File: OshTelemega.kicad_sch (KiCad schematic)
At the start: 138 parts, among them J1 USB_C_Receptacle_USB2.0_16P, J10 SERVOS, J12 DEBUG, J2 Conn_02x04_Counter_Clockwise, J3 SMA_Edgelaunch, J4 USB_C_Receptacle_USB2.0_16P, J5 UFL, J6 RIGHT, J7 LEFT, J8 Conn_01x02, U1 STM32L151VCTx, U10 MMC5983MA, U11 TSM200N03, U12 LM293QT, U13 LM293QT, U14 TSM200N03, U15 LM293QT, U16 TSM200N03, U17 MCP73831-2-OT, U18 TC2185-3.3VxCTTR, U2 WE-TVS-82400102, U3 ADXL375, U4 MS5607-02BA, U5 MAX-M10S, U6 MCP130-xxxxTT, U7 W25Q64JVXGIQ, U8 CC1200, U9 BMI088, Y1 ABM8W-40.0000MHZ

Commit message: v0.1 done. Redesigning for potential mosaic integration
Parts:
- removed BZ1: Buzzer, Buzzer_Beeper:Buzzer_TDK_PS1240P02BT_D12.2mm_H6.5mm, symbol Device:Buzzer
- removed J1: USB_C_Receptacle_USB2.0_16P, Connector_USB:USB_C_Receptacle_GCT_USB4105-xx-A_16P_TopMnt_Horizontal, symbol Connector:USB_C_Receptacle_USB2.0_16P
- removed U7: W25Q64JVXGIQ, FCU2025Lib:DFN_XGIQ TR_WIN, symbol Memory_Flash:W25Q32JVSS
- added H5: MountingHole_Pad, MountingHole:MountingHole_3.2mm_M3_DIN965_Pad, symbol Mechanical:MountingHole_Pad
- added U19: W25Q64JVXGIQ, FCU2025Lib:DFN_XGIQ TR_WIN, symbol Memory_Flash:W25Q128JVP
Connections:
- net +3V3: now also U19.3 (~{WP}/IO_{2}), U19.7 (~{HOLD}/~{RESET}/IO_{3}), U19.8 (VCC)
- net CS_COMP0: now also J2.8 (Pin_8); no longer J2.6 (Pin_6)
- net CS_COMP1: now also J2.6 (Pin_6); no longer J2.5 (Pin_5)
- net CS_FLASH: now also U19.1 (~{CS})
- net FET_C: now also R27.1, U14.7_8 (D); no longer R23.1, U14.5_6 (D)
- net FET_D: now also R23.1, U14.5_6 (D); no longer R27.1, U14.7_8 (D)
- net FIRE_C: now also R25.2, R26.1; no longer R21.2, R22.1
- net FIRE_D: now also R21.2, R22.1; no longer R25.2, R26.1
- net GATE_C: now also R26.2, U14.2 (G); no longer R22.2, U14.4 (G)
- net GATE_D: now also R22.2, U14.4 (G); no longer R26.2, U14.2 (G)
- net GATE_E: now also U15.7 (OUT2); no longer U15.1 (OUT1)
- net GATE_F: now also U15.1 (OUT1); no longer U15.7 (OUT2)
- net GND: now also J4.A1 (GND), J4.A12 (GND), J4.B1 (GND), J4.B12 (GND), J4.S1 (SHIELD), H5.1, U19.4 (GND), U19.9 (EP)
- net MISO2: now also U19.2 (DO/IO_{1})
- net MOSI2: now also J2.5 (Pin_5), U19.5 (DI/IO_{0}); no longer J2.3 (Pin_3)
- net NRST: now also J12.4 (Pin_4); no longer J12.2 (Pin_2)
- net SCK2: now also U19.6 (CLK)
- net SENSE_C: now also R27.2, R28.2; no longer R23.2, R24.2
- net SENSE_D: now also R23.2, R24.2; no longer R27.2, R28.2
- net SWCLK: now also J12.2 (Pin_2); no longer J12.4 (Pin_4)
- net VBUS: now also J4.A4 (VBUS), J4.A9 (VBUS), J4.B4 (VBUS), J4.B9 (VBUS)
- net V_LIPO: now also J2.3 (Pin_3); no longer J2.8 (Pin_8)
- net at R1.1: now also J4.A5 (CC1)
- net at R10.1: now also J4.A6 (D+), J4.B6 (D+)
- net at R9.1: now also J4.A7 (D-), J4.B7 (D-)
- net at R2.1: now also J4.B5 (CC2)
- net at R6.2: now also J10.4 (Pin_4); no longer J10.3 (Pin_3)
- net at R7.2: now also J10.3 (Pin_3); no longer J10.4 (Pin_4)
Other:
- moved on the sheet: J4

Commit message: before adding 10 pin companion
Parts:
- removed J12: DEBUG, Connector_PinHeader_1.27mm:PinHeader_2x02_P1.27mm_Vertical, symbol Connector_Generic:Conn_02x02_Counter_Clockwise
- added J1: Conn_ARM_SWD_TagConnect_TC2030-NL, Connector:Tag-Connect_TC2030-IDC-NL_2x03_P1.27mm_Vertical, symbol Connector:Conn_ARM_SWD_TagConnect_TC2030-NL
- added J9: Conn_02x05_Counter_Clockwise, Connector_PinHeader_1.27mm:PinHeader_2x05_P1.27mm_Vertical, symbol Connector_Generic:Conn_02x05_Counter_Clockwise
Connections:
- net +3V3: now also J1.1 (VCC)
- net GND: now also J1.5 (GND)
- net NRST: now also J1.3 (~{RESET})
- net SWCLK: now also J1.4 (SWCLK)
- net SWDIO: now also J1.2 (SWDIO)
- net TX1: now reaches U1.68 (PA9)
- net RX1: now reaches U1.69 (PA10)
- no-connect marks 35 -> 33
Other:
- moved on the sheet: J10, J2, J6, J7, R5

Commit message: v0.2 done - just needs review and silkscreens
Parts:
- removed FL1: B39162B4300F210, Filter:Filter_1411-5_1.4x1.1mm, symbol Filter:SAFFA1G96FN0F0A
- removed J2: Conn_02x04_Counter_Clockwise, Connector_PinHeader_1.27mm:PinHeader_2x04_P1.27mm_Vertical, symbol Connector_Generic:Conn_02x04_Counter_Clockwise
- added C43: 10nF X7R, Capacitor_SMD:C_0402_1005Metric, symbol Device:C
- added C44: 0.1uF, Capacitor_SMD:C_0402_1005Metric, symbol Device:C
- added D2: BAT54CW, Package_TO_SOT_SMD:SOT-323_SC-70, symbol Diode:BAT54CW
- added D5: LED_Dual_AAKK, LED_SMD:LED_LiteOn_LTST-C19HE1WT, symbol Device:LED_Dual_AAKK
- added FB2: LQG15HS47NJ02, Inductor_SMD:L_0402_1005Metric, symbol Device:FerriteBead
- added J2: Conn_01x02, Connector_PinHeader_1.27mm:PinHeader_1x02_P1.27mm_Vertical, symbol Connector_Generic:Conn_01x02
- added Q1, Q3: SiA449DJ, Package_TO_SOT_SMD:Vishay_PowerPAK_SC70-6L_Single, symbol Transistor_FET:SiA449DJ
- added Q2: AO3400A, Package_TO_SOT_SMD:SOT-23, symbol Transistor_FET:AO3400A
- added R49, R52, R53: 100k, Resistor_SMD:R_0402_1005Metric, symbol Device:R
- added R50, R51: 1k, Resistor_SMD:R_0402_1005Metric, symbol Device:R
- added R54: 10R 0.25W, Resistor_SMD:R_0402_1005Metric, symbol Device:R
- added U21: SN74LVC1G80QDCKTQ1, Package_TO_SOT_SMD:SOT-353_SC-70-5, symbol 74xGxx:74LVC1G80
- added U7: DRV5012AEDMRR, Package_SON:Texas_X2SON-4-1EP_1.1x1.4mm_P0.5mm_EP0.8x0.6mm, symbol FCU2025:DRV5012AEDMRR
- C21: footprint Inductor_SMD:L_0402_1005Metric -> Capacitor_SMD:C_0402_1005Metric
- FB1: value FerriteBead -> LI0402C221R-10
- J1: value Conn_ARM_SWD_TagConnect_TC2030-NL -> TAGCONNECT
- J8: value Conn_01x02 -> BATT
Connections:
- net +3V3: now also J9.3 (Pin_3)
- net BUZZ: now also J2.1 (Pin_1)
- net CS_COMP0: now also J9.10 (Pin_10)
- net CS_COMP1: now also J9.8 (Pin_8)
- net GND: now also J9.1 (Pin_1), C43.2, C44.1, D5.3 (K1), D5.4 (K2), J2.2 (Pin_2), Q2.2 (S), R49.1, R52.1, U21.3 (GND), U7.2 (GND), U7.4 (SEL), U7.5 (PAD)
- net MGSW_IN: now also C44.2, Q3.1 (D), R53.2, U21.5 (VCC), U7.1 (VCC)
- net MISO2: now also J9.4 (Pin_4)
- net MOSI2: now also J9.7 (Pin_7)
- net RX1: now also J9.6 (Pin_6)
- net SCK2: now also J9.2 (Pin_2)
- net TX1: now also J9.5 (Pin_5)
- net V_CHARGE: now also Q1.1 (D); no longer J7.8 (Pin_8)
- net V_LIPO: now also C23.2, D1.1 (K), J9.9 (Pin_9), R40.2, U18.1 (VIN), U18.3 (ON/~{OFF}); no longer D1.2 (A)
- net at U5.11 (RF_IN): now also J5.1 (In), FB2.1
- net at U5.14 (VCC_RF): now also R54.1
- new net: Q2.3 (D), Q3.3 (G), R53.1
- new net: C43.1, FB2.2, R54.2
- new net: D5.2 (A2), R51.1
- new net: D2.2, R51.2, U21.1 (D), U21.4 (~{Q})
- new net: Q1.3 (G), R49.2
- new net: D5.1 (A1), R50.1
- new net: D2.3, Q2.1 (G), R52.2
- new net HALL_OUT: D2.1, R50.2, U21.2 (C), U7.3 (OUT)
- new net MGSW_OUT: D1.2 (A), Q3.4 (S)
- new net V_PROT: J7.8 (Pin_8), Q1.4 (S)
- no-connect marks 33 -> 32
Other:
- moved on the sheet: C22, C23, C24, D1, J1, J10, J5, J6, J7, J8, J9, R40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

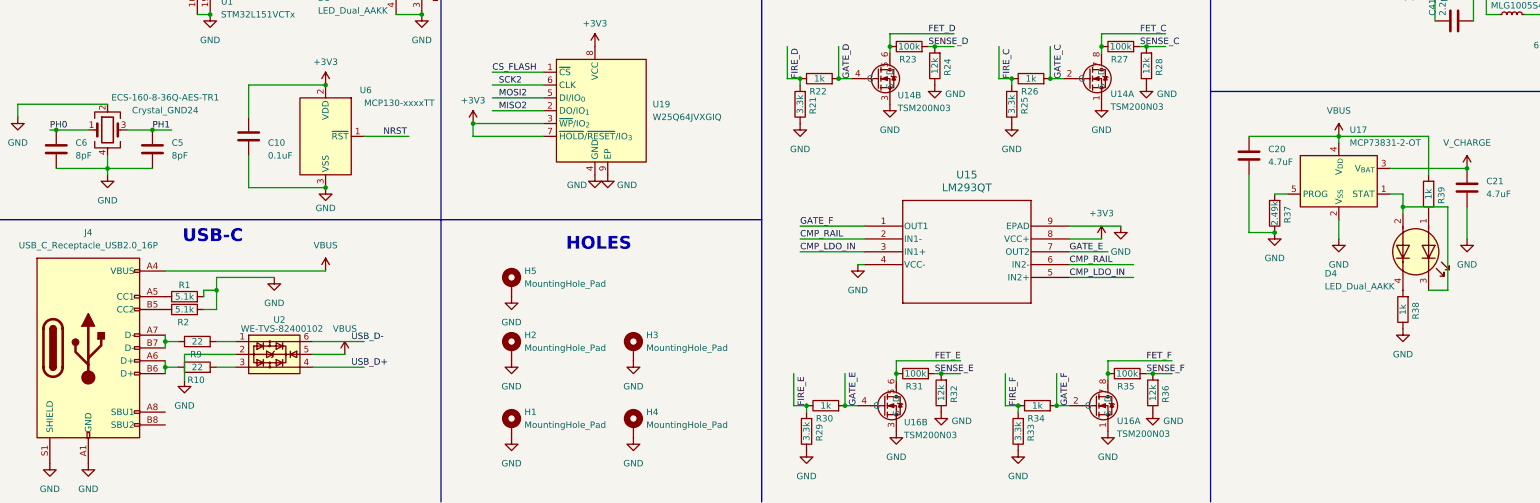
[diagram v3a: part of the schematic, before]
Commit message: some jlc manufacturing considerations
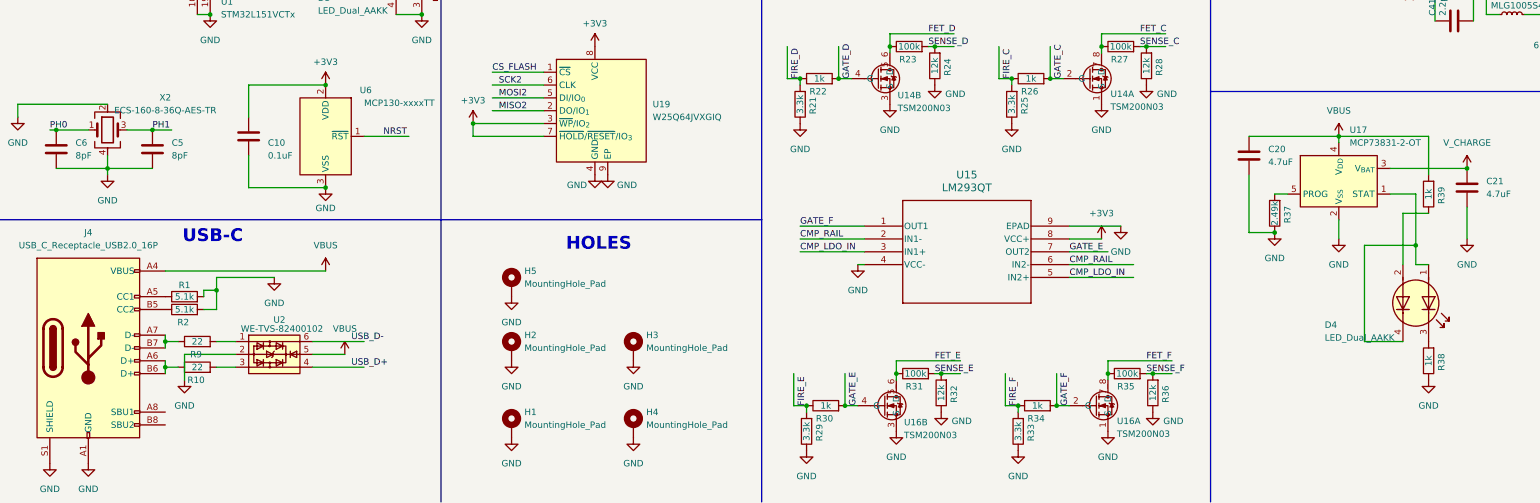
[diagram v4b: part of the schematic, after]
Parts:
- D3, D4, D5: footprint LED_SMD:LED_LiteOn_LTST-C19HE1WT -> FCU2025Lib:DualLED0606
- X2: renamed from ECS-160-8-36Q-AES-TR1; value Crystal_GND24 -> ECS-160-8-36Q-AES-TR
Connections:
- net at D4.1 (A1): now also D4.4 (K2), U17.1 (STAT); no longer R39.1
- net at R38.2: now also D4.3 (K1); no longer D4.4 (K2)
- new net: D4.2 (A2), R39.1
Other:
- moved on the sheet: R38

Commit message: fixed wrong orientation on mag switch mosfet
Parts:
- X2: value ECS-160-8-36Q-AES-TR -> ECS-160-8-36Q-AES-TR1
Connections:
- net MGSW_IN: now also Q3.4 (S); no longer Q3.1 (D)
- net MGSW_OUT: now also Q3.1 (D); no longer Q3.4 (S)
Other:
- moved on the sheet: Q3
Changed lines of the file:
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@@
 			)
 		)
-		(property "Value" "ECS-160-8-36Q-AES-TR"
+		(property "Value" "ECS-160-8-36Q-AES-TR1"
 			(at 46.99 206.9398 0)
 			(effects
@@
 		(on_board yes)
 		(dnp no)
-		(fields_autoplaced yes)
 		(property "Reference" "Q1"
 			(at 345.44 212.09 90)
@@
 	(symbol
 		(lib_id "Transistor_FET:SiA449DJ")
-		(at 439.42 280.67 90)
+		(at 439.42 280.67 270)
+		(mirror x)
 		(unit 1)
 		(exclude_from_sim no)
@@
 		(on_board yes)
 		(dnp no)
-		(fields_autoplaced yes)
 		(property "Reference" "Q3"
 			(at 439.42 271.78 90)
@@
 		)
 		(property "Footprint" "Package_TO_SOT_SMD:Vishay_PowerPAK_SC70-6L_Single"
-			(at 441.325 275.59 0)
+			(at 437.515 275.59 0)
 			(effects
 				(font
@@
 		)
 		(property "Datasheet" "http://www.vishay.com/docs/62644/sia449dj.pdf"
-			(at 443.23 275.59 0)
+			(at 435.61 275.59 0)
 			(effects
 				(font

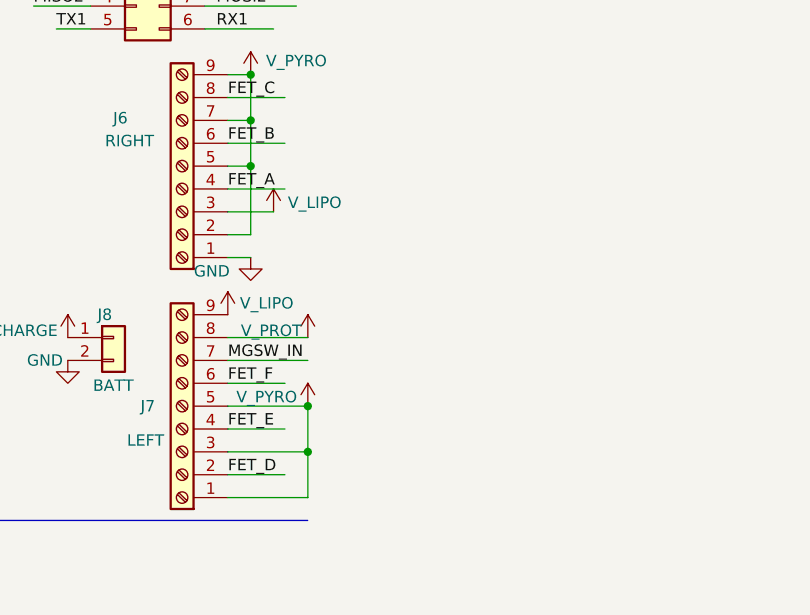
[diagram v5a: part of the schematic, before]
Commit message: added pyro rp protection
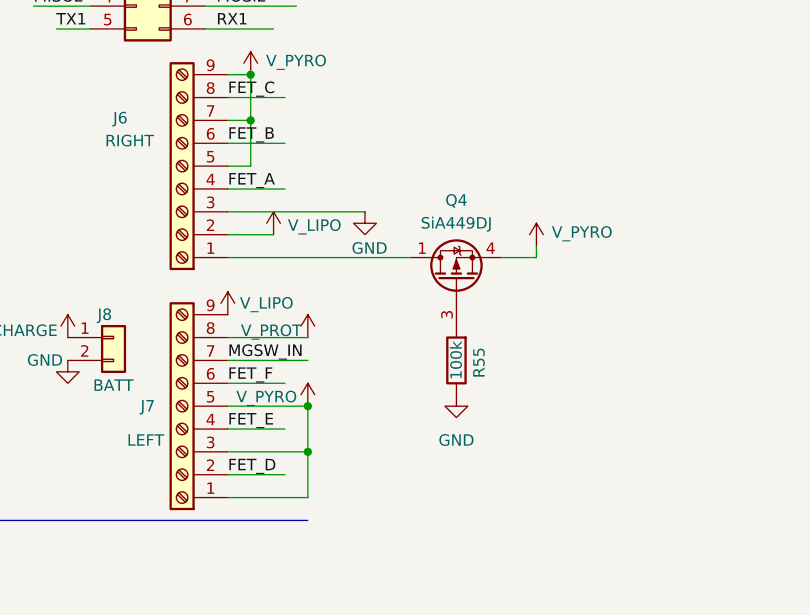
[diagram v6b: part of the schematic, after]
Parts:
- added Q4: SiA449DJ, Package_TO_SOT_SMD:Vishay_PowerPAK_SC70-6L_Single, symbol Transistor_FET:SiA449DJ
- added R55: 100k, Resistor_SMD:R_0402_1005Metric, symbol Device:R
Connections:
- net GND: now also J6.3 (Pin_3), R55.1; no longer J6.1 (Pin_1)
- net V_LIPO: now also J6.2 (Pin_2); no longer J6.3 (Pin_3)
- net V_PYRO: now also Q4.4 (S); no longer J6.2 (Pin_2)
- new net: J6.1 (Pin_1), Q4.1 (D)
- new net: Q4.3 (G), R55.2

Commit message: drc changes and more ground stitching
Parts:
- removed U11, U14, U16: TSM200N03, FCU2025Lib:8-PDFN (3x3), symbol FCU2025:TSM200N03
- added U20, U22, U23: SISB46DN, FCU2025Lib:PowerPak1212-8-Dual, symbol FCU2025:SI7232DN
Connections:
- net FET_A: now also U20.6 (D)
- net FET_B: now also U20.5 (D)
- net FET_C: now also U22.5 (D)
- net FET_D: now also U22.6 (D)
- net FET_E: now also U23.6 (D)
- net FET_F: now also U23.5 (D)
- net GATE_A: now also U20.4 (G)
- net GATE_B: now also U20.2 (G)
- net GATE_C: now also U22.2 (G)
- net GATE_D: now also U22.4 (G)
- net GATE_E: now also U23.4 (G)
- net GATE_F: now also U23.2 (G)
- net GND: now also U20.1 (S), U20.3 (S), U22.1 (S), U22.3 (S), U23.1 (S), U23.3 (S)
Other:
- moved on the sheet: C22, C23, C24, D1, J2, R40, R41, R42, R43, R44, R45, R46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

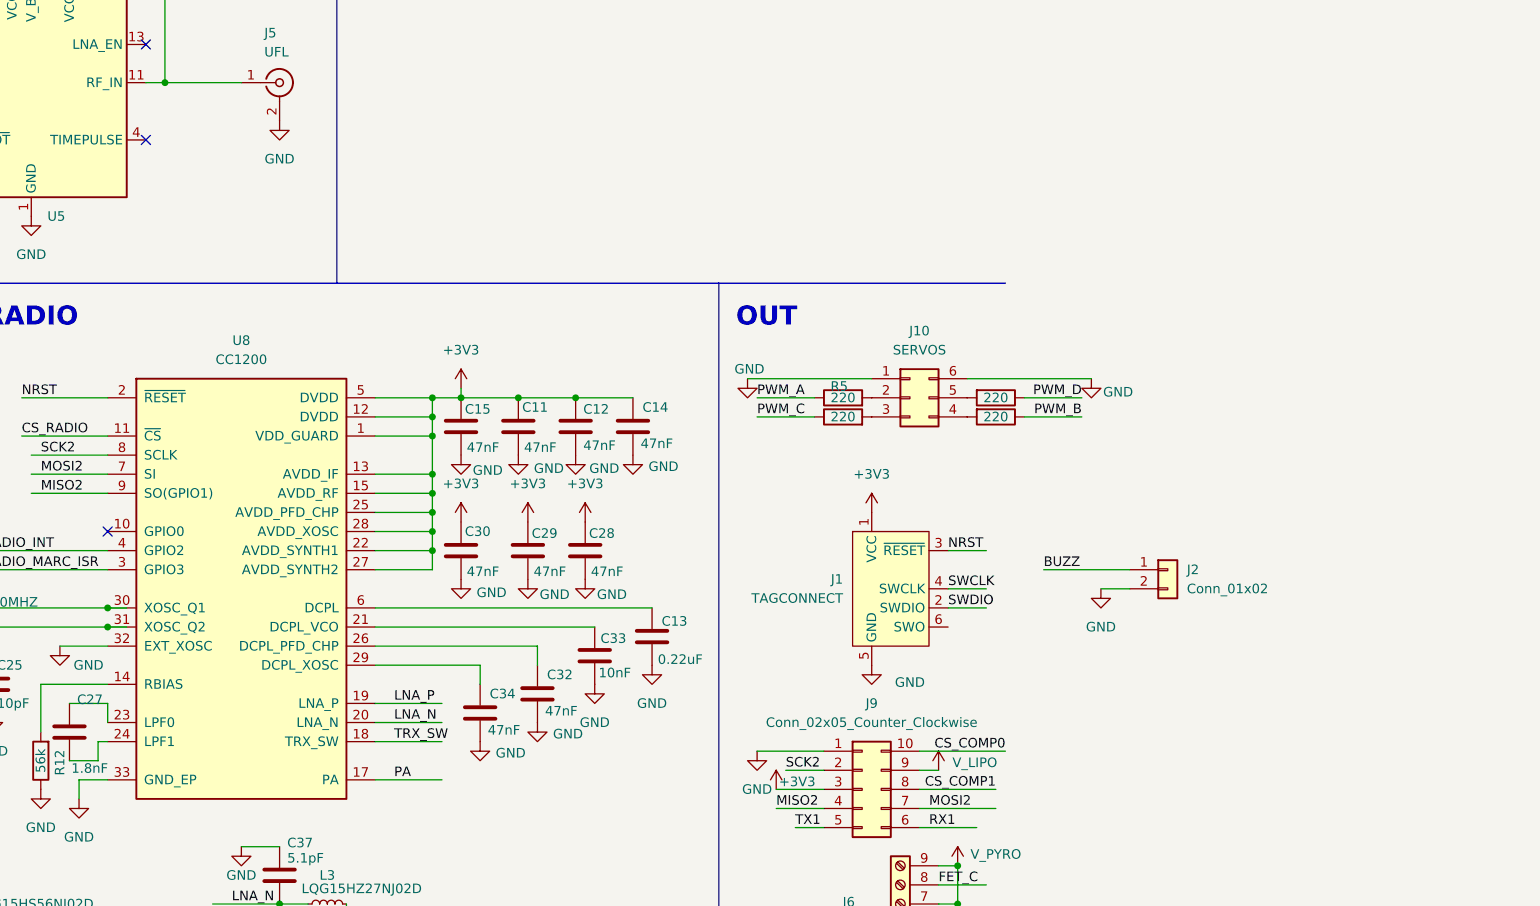
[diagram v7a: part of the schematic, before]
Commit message: resolved drc, added buzzer, and PPS led
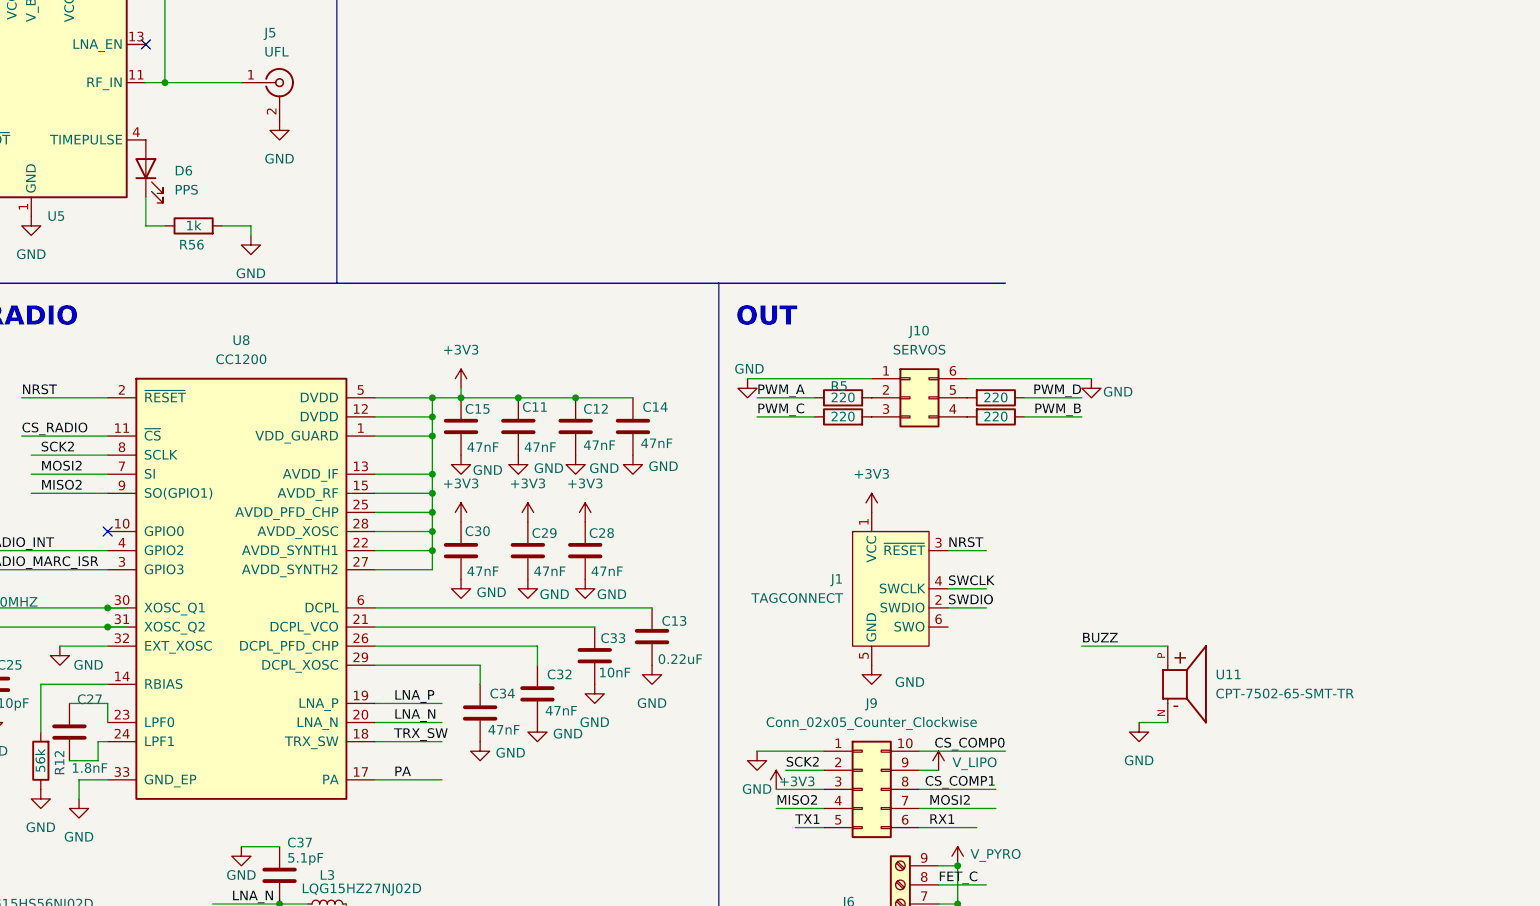
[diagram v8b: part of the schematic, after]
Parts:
- removed J2: Conn_01x02, Connector_PinHeader_1.27mm:PinHeader_1x02_P1.27mm_Vertical, symbol Connector_Generic:Conn_01x02
- added D6: PPS, LED_SMD:LED_0402_1005Metric, symbol Device:LED
- added R56: 1k, Resistor_SMD:R_0402_1005Metric, symbol Device:R
- added U11: CPT-7502-65-SMT-TR, FCU2025Lib:XDCR_CPT-7502-65-SMT-TR, symbol FCU2025:CPT-7502-65-SMT-TR
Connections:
- net BUZZ: now also U11.P
- net GND: now also R56.2, U11.N
- net at U5.4 (TIMEPULSE): now also D6.2 (A)
- new net: D6.1 (K), R56.1
- no-connect marks 32 -> 31
